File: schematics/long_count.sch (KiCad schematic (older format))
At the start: 50 parts, among them J1 CONN_01X06, J2 BARREL_JACK, SW1 Rotary_Encoder, SW2 SW_Push, SW3 SW_Push, SW4 SW_Push, U1 PIC18F27K40, U2 LM350T, U3 CD74HC154M96, Y1 Crystal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

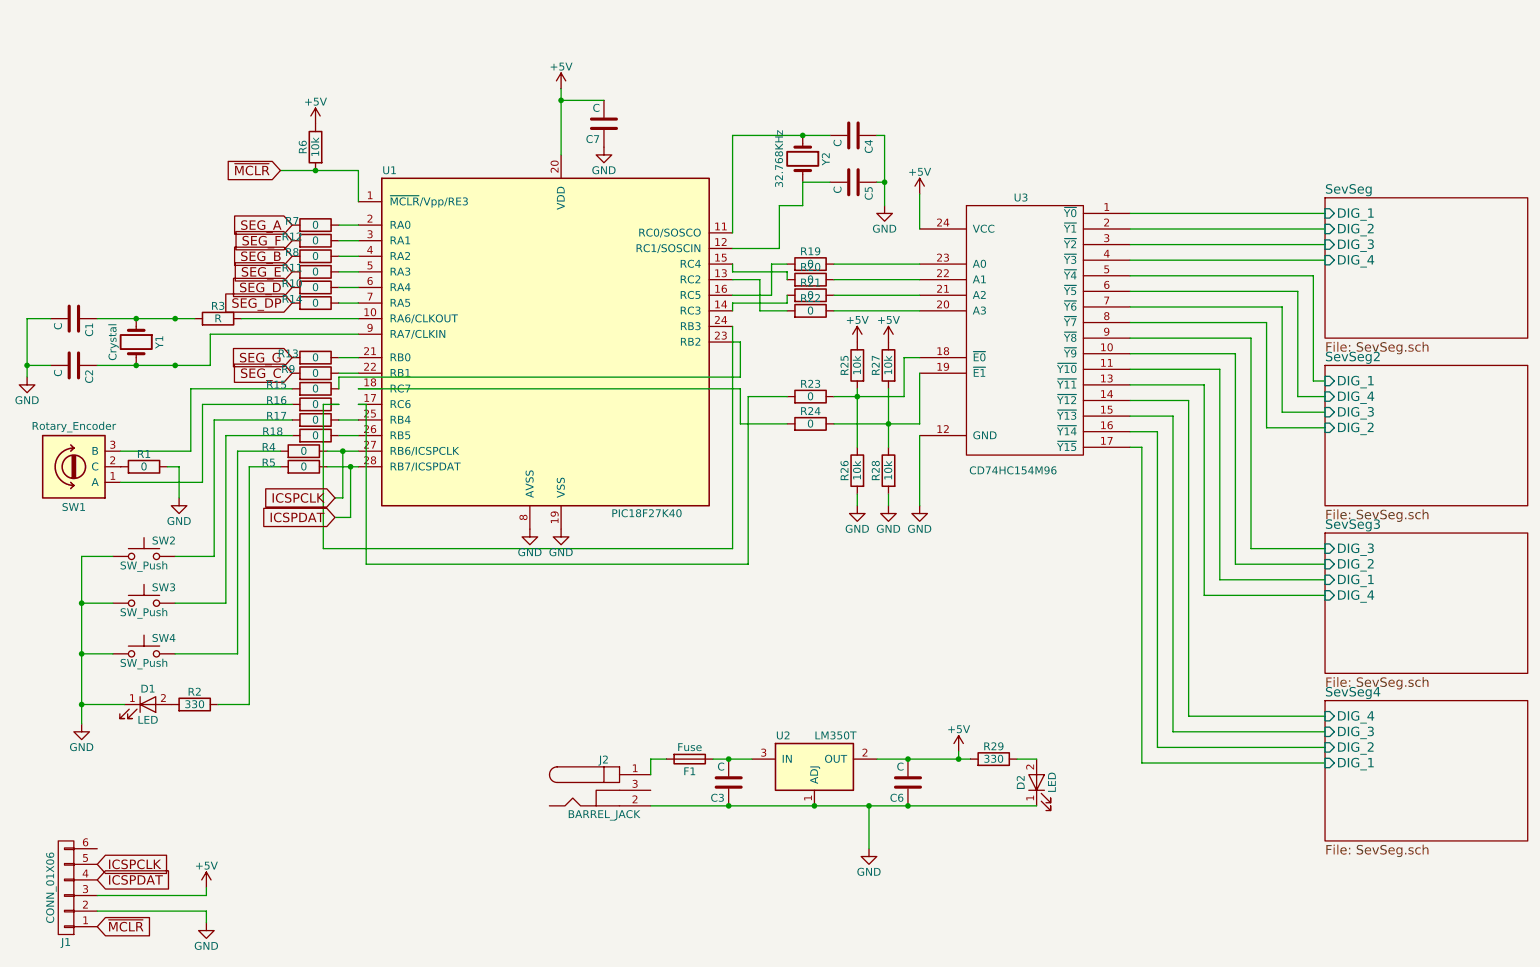
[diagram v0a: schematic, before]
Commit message: Clean up schematic
More readable, some notes on components and decisions, and a proper
linear regulator. 7805 4lyfe.
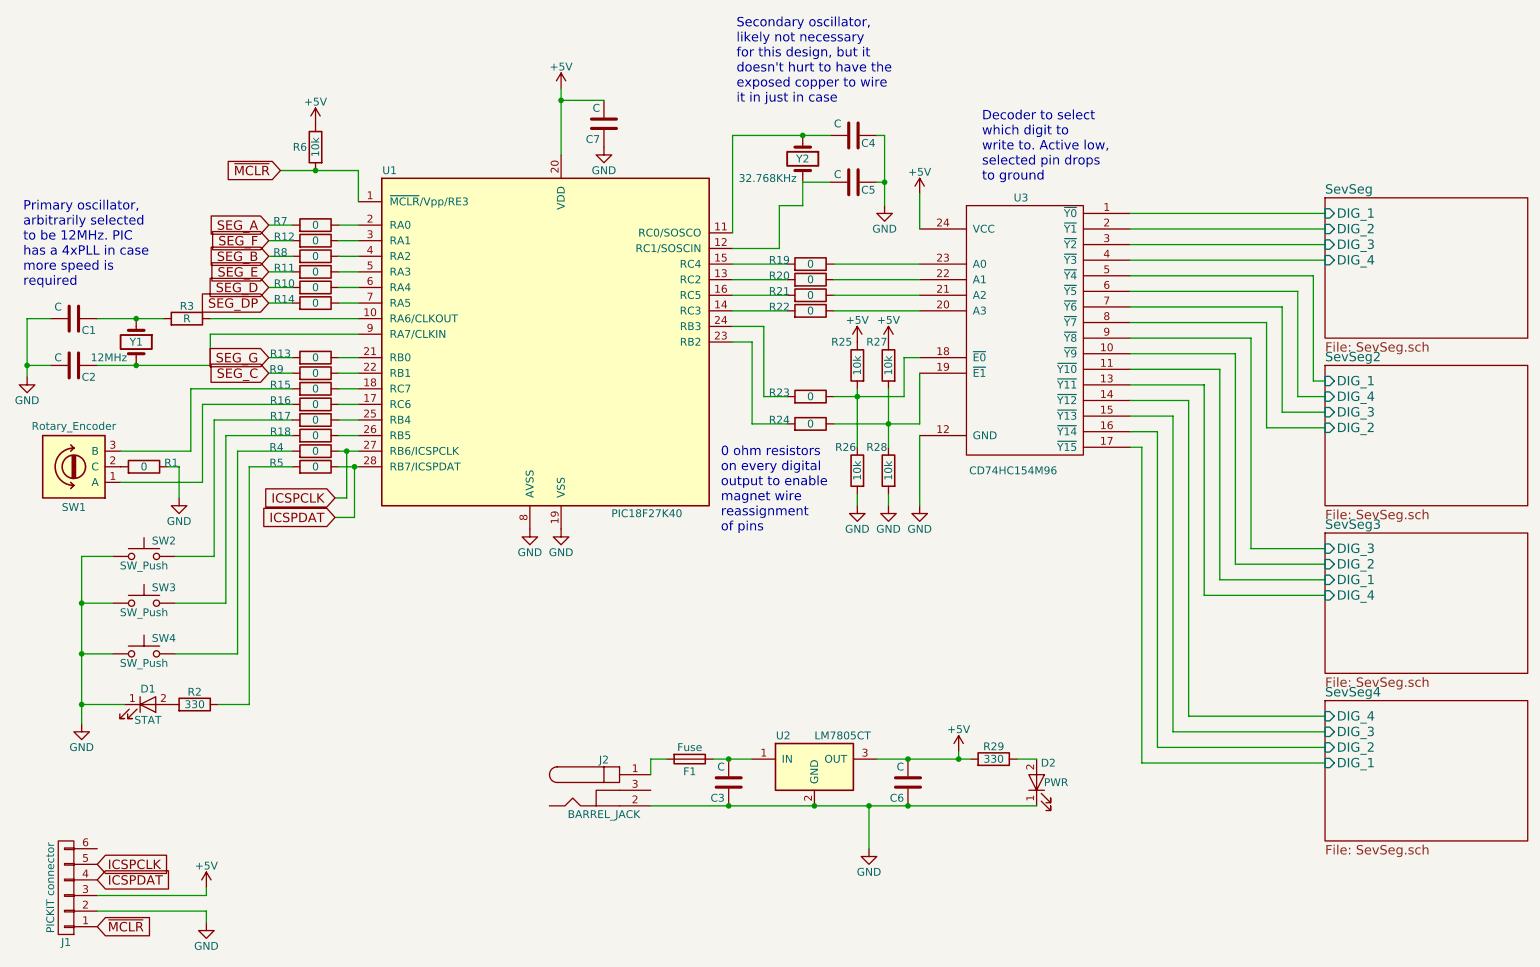
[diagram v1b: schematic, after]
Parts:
- removed U2: LM350T, TO_SOT_Packages_THT:TO-220-3_Vertical, symbol LM350T
- added U2: LM7805CT, TO_SOT_Packages_THT:TO-220-3_Vertical, symbol LM7805CT
- D1: value LED -> STAT
- D2: value LED -> PWR
- J1: value CONN_01X06 -> PICKIT connector
- Y1: value Crystal -> 12MHz
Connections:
- net +5V: now also U2.3 (OUT)
- net GND: now also U2.2 (GND)
- net at U1.13 (RC2): now also R20.2; no longer R22.2
- net at U1.14 (RC3): now also R22.2; no longer R21.2
- net at U1.15 (RC4): now also R19.2; no longer R20.2
- net at U1.16 (RC5): now also R21.2; no longer R19.2
- net at U1.17 (RC6): now also R16.1; no longer R23.2
- net at U1.18 (RC7): now also R15.1; no longer R24.2
- net at U1.23 (RB2): now also R24.2; no longer R15.1
- net at U1.24 (RB3): now also R23.2; no longer R16.1
- net at C3.2, F1.1: now also U2.1 (IN)
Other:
- note added: "0 ohm resistors \non every digital \noutput to enable \nmagnet wire \nreassignment \nof pins"
- note added: "Decoder to select \nwhich digit to \nwrite to. Active low,\nselected pin drops \nto ground\n"
- note added: "Primary oscillator,\narbitrarily selected\nto be 12MHz. PIC\nhas a 4xPLL in case\nmore speed is\nrequired"
- note added: "Secondary oscillator,\nlikely not necessary\nfor this design, but it\ndoesn't hurt to have the\nexposed copper to wire\nit in just in case"
- moved on the sheet: R3, R4, R5

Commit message: Add test points for VDD and VSS
Also add center positive polarity symbol for DC input
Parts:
- added J3: VDD, Pin_Headers:Pin_Header_Straight_1x01_Pitch2.54mm, symbol TEST_1P
- added J4: VSS, Pin_Headers:Pin_Header_Straight_1x01_Pitch2.54mm, symbol TEST_1P
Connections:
- net +5V: now also J3.1
- net GND: now also J4.1
